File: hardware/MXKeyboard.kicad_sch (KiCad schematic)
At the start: 4 parts

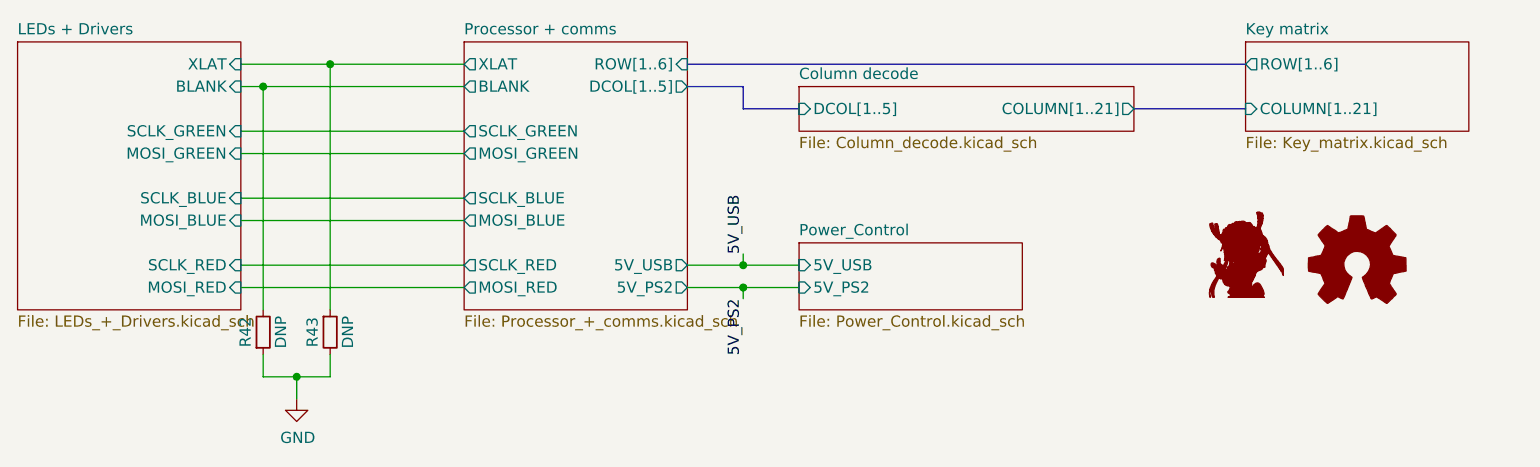
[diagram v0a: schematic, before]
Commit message: Improved a pile of the schematic, converting it to use KiCad schematic symbols and footprints instead of eagle imports
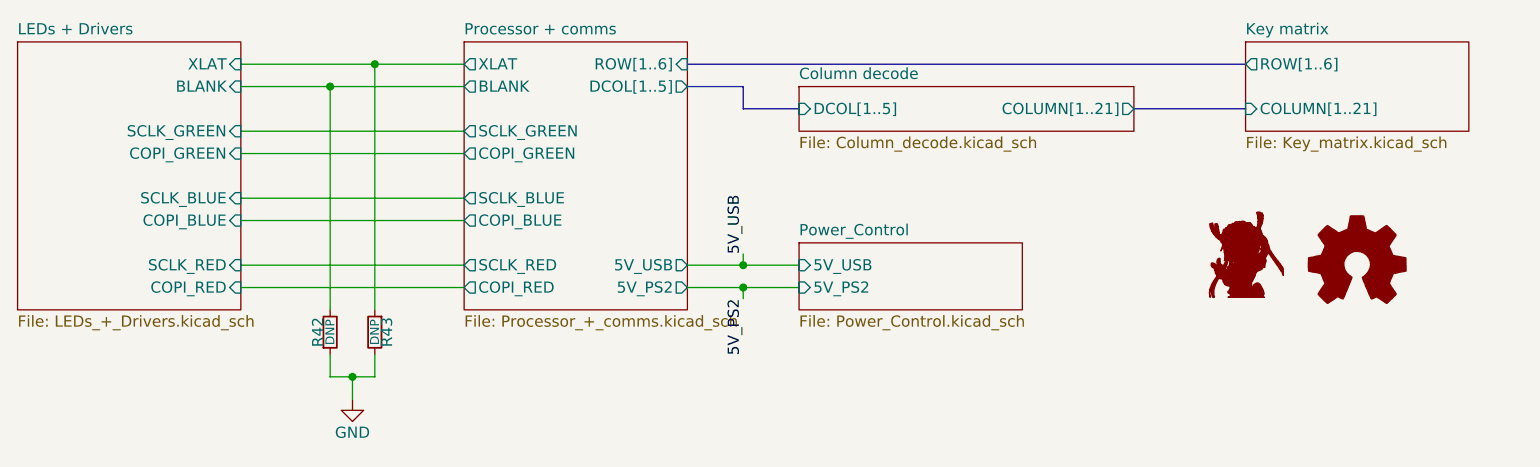
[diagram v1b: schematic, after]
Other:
- sheet LEDs + Drivers ports: added COPI_BLUE, COPI_GREEN, COPI_RED; removed MOSI_BLUE, MOSI_GREEN, MOSI_RED
- sheet Processor + comms ports: added COPI_BLUE, COPI_GREEN, COPI_RED; removed MOSI_BLUE, MOSI_GREEN, MOSI_RED
- moved on the sheet: R42, R43
